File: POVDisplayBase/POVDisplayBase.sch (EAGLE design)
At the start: 35 parts, among them IC1 317EMP, IC2 STM32L052C8T, J1 FTSH-105, Q1 SSM3K329R, Q2 FQD10N20L, X1 MINI-USB-UX60-MB-5ST

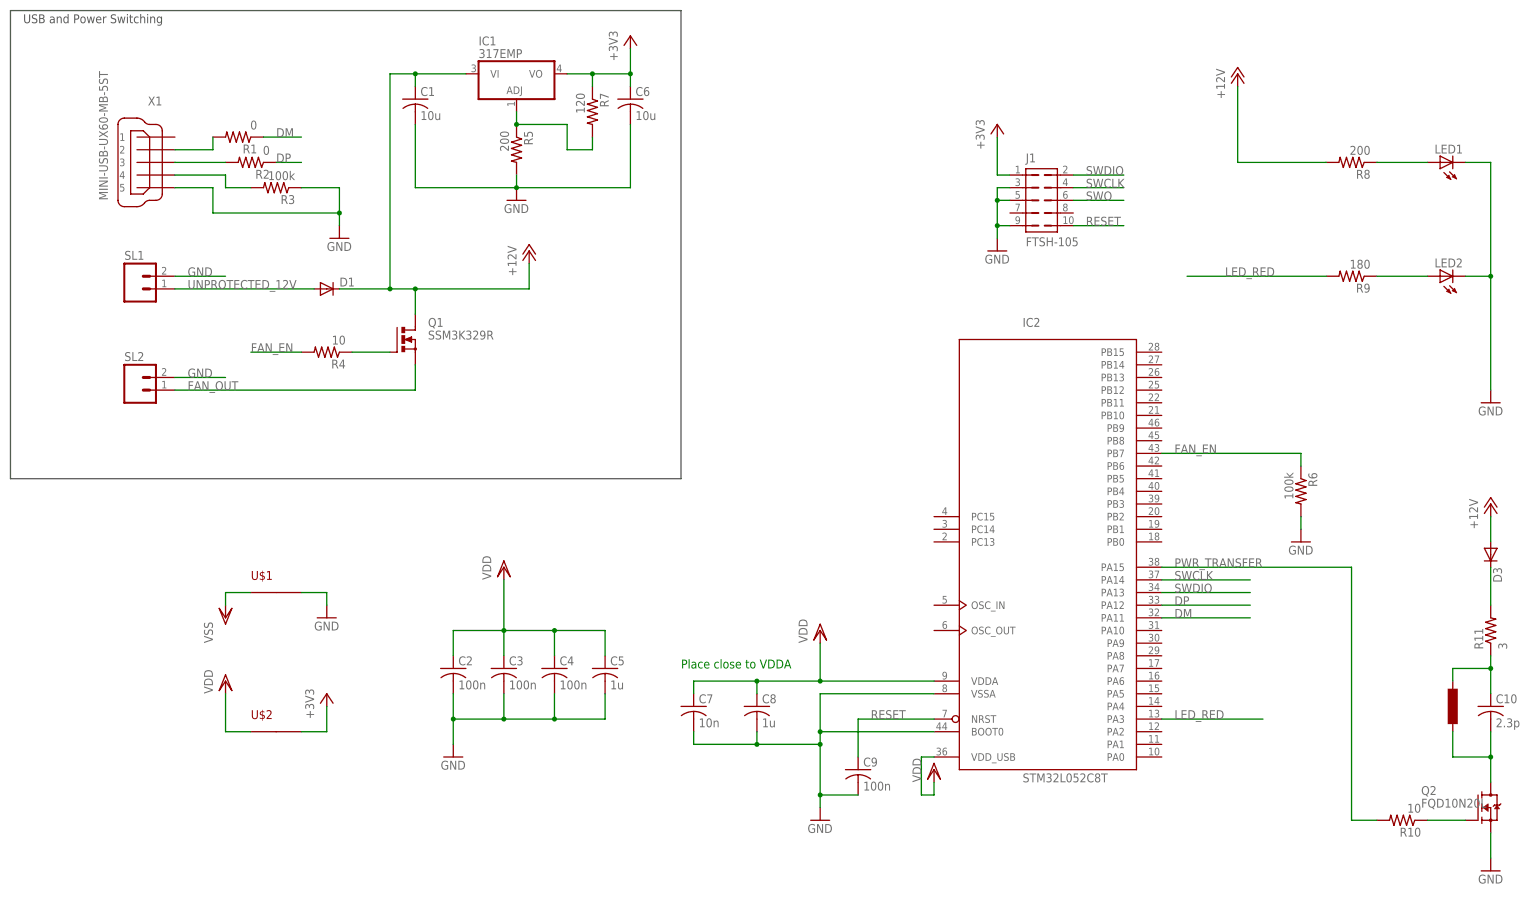
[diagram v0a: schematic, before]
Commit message: Removed the processor and simplified the POVDisplayBase
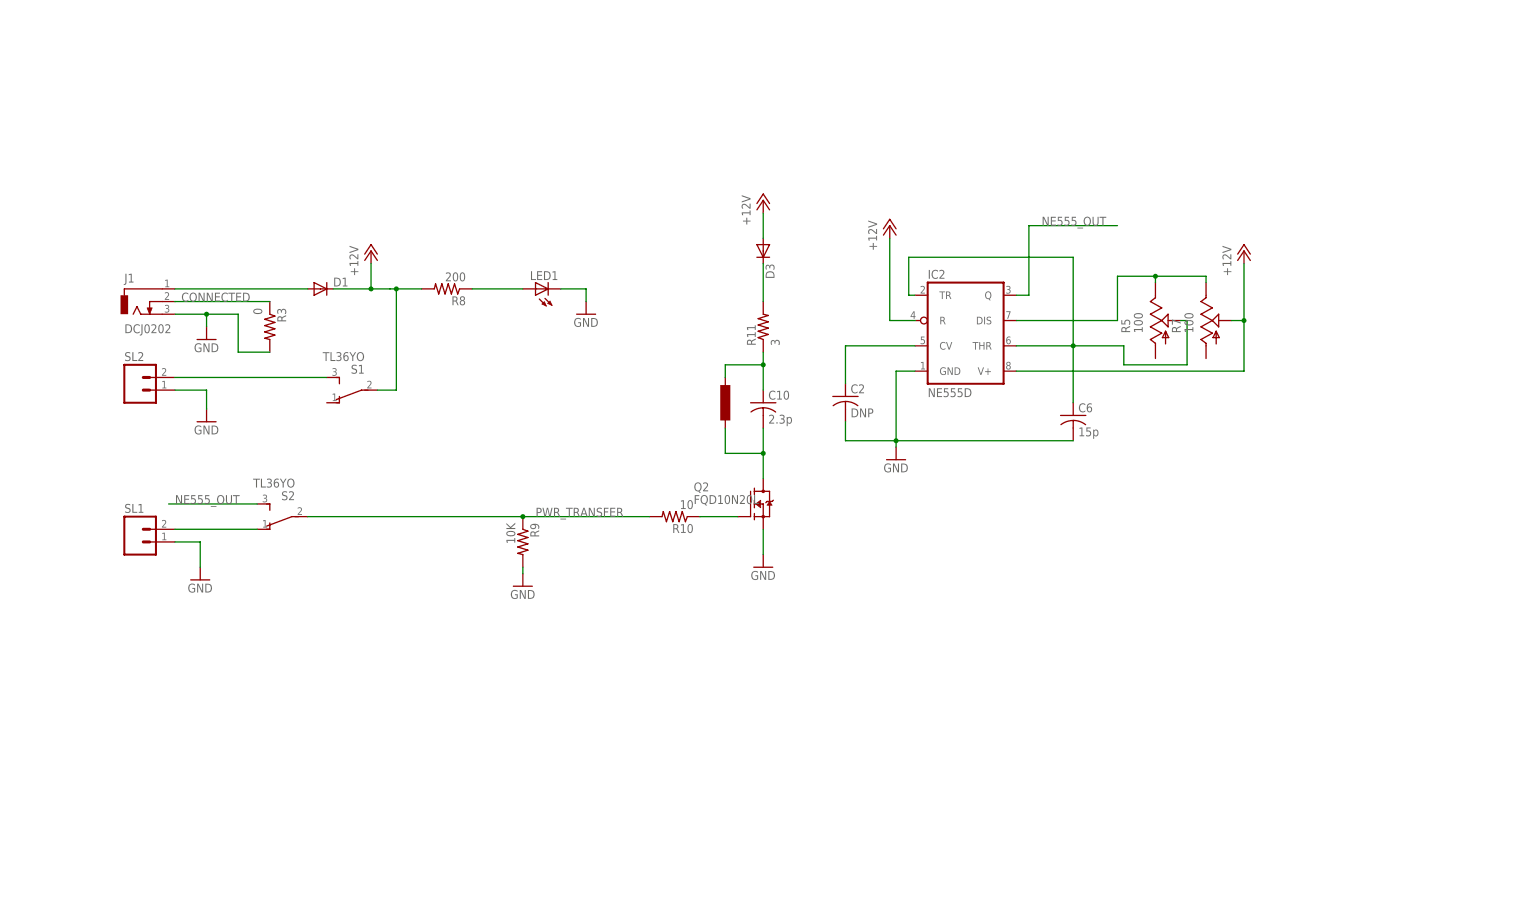
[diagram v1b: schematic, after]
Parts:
- removed C1: 10u, resistor:C-USC0603
- removed C3, C4, C9: 100n, resistor:C-USC0603
- removed C5, C8: 1u, resistor:C-USC0603
- removed C7: 10n, resistor:C-USC0603
- removed IC1: 317EMP, linear:317EMP
- removed LED2: (no value), led:LEDCHIP-LED0603
- removed Q1: SSM3K329R, NicksParts:SSM3K329R
- removed R1, R2: 0, resistor:R-US_R0603
- removed R4: 10, resistor:R-US_R0603
- removed R6: 100k, resistor:R-US_R0603
- removed U$1, U$2: SHORT, NicksParts:SHORT
- removed X1: MINI-USB-UX60-MB-5ST, con-hirose:MINI-USB-UX60-MB-5ST
- added S1, S2: TL36YO, switch:TL36YO
- C2: value 100n -> DNP
- C6: value 10u -> 15p
- IC2: value STM32L052C8T -> NE555D; device micro-stm_v2:STM32L052C8T -> linear:NE555D; DIGIKEY 497-14903-ND -> 296-6501-1-ND
- J1: value FTSH-105 -> DCJ0202; device NicksParts:FTSH-105 -> con-jack:DCJ0202; DIGIKEY SAM1161-50-ND -> CP-002B-ND; MATING_CONN (none) -> CP3-1001-ND
- R3: value 100k -> 0; DIGIKEY P100KGCT-ND -> P180GCT-ND
- R5: value 200 -> 100; device resistor:R-US_R0603 -> pot:TRIM_US-3223J; DIGIKEY P0.0GCT-ND -> A106082CT-ND
- R7: value 120 -> 100; device resistor:R-US_R0603 -> pot:TRIM_US-3223J; DIGIKEY P0.0GCT-ND -> A106082CT-ND
- R9: value 180 -> 10K
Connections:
- removed net +3V3: C6.1, IC1.VO, J1.1, R7.1, U$2.P$2
- removed net DM: IC2MCU.PA11, R1.1
- removed net DP: IC2MCU.PA12, R2.1
- removed net FAN_EN: IC2MCU.PB7, R4.2, R6.1
- removed net FAN_OUT: Q1.S, SL2.1
- removed net LED_RED: IC2MCU.PA3, R9.2
- removed net N$10: Q1.G, R4.1
- removed net N$6: R3.2, X1.4
- removed net N$7: IC1.ADJ, R5.1, R7.2
- removed net RESET: C9.1, IC2MCU.NRST, J1.10
- removed net SWCLK: IC2MCU.PA14, J1.4
- removed net SWDIO: IC2MCU.PA13, J1.2
- removed net SWO: J1.6
- removed net UNPROTECTED_12V: D1.A, SL1.1
- removed net VDD: C2.1, C3.1, C4.1, C5.1, C7.1, C8.1, IC2MCU.VDDA, IC2MCU.VDD_USB, U$2.P$1
- removed net VSS: U$1.P$1
- new net CONNECTED: J1.2, R3.1
- new net N$13: S2.O, SL1.2
- new net N$14: C2.1, IC2.CV
- new net N$3: S1.S, SL2.2
- new net NE555_OUT: IC2.Q, S2.S
- net +12V: now also IC2.R, IC2.V+, R7.S, S1.P; no longer C1.1, IC1.VI, Q1.D
- net GND: now also IC2.GND, R3.2, R9.2, SL1.1, SL2.1; no longer C1.2, C3.2, C4.2, C5.2, C7.2, C8.2, C9.2, IC2MCU.BOOT0, IC2MCU.VSSA, J1.5, J1.9, LED2.C, R3.1, R5.2, R6.2, SL1.2, SL2.2, U$1.P$2, X1.5
- net N$4: now also D1.A, J1.1; no longer R2.2, X1.3
- net N$5: now also C6.1, IC2.THR, IC2.TR, R5.S; no longer R1.2, X1.2
- net N$9: now also IC2.DIS, R5.E, R7.E; no longer LED2.A, R9.1
- net PWR_TRANSFER: now also R9.1, S2.P; no longer IC2MCU.PA15
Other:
- note removed: "Place close to VDDA"
- note removed: "USB and Power Switching"
- moved on the sheet: C10, C2, C6, D1, D3, LED1, Q2, R10, R11, R3, R8, R9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

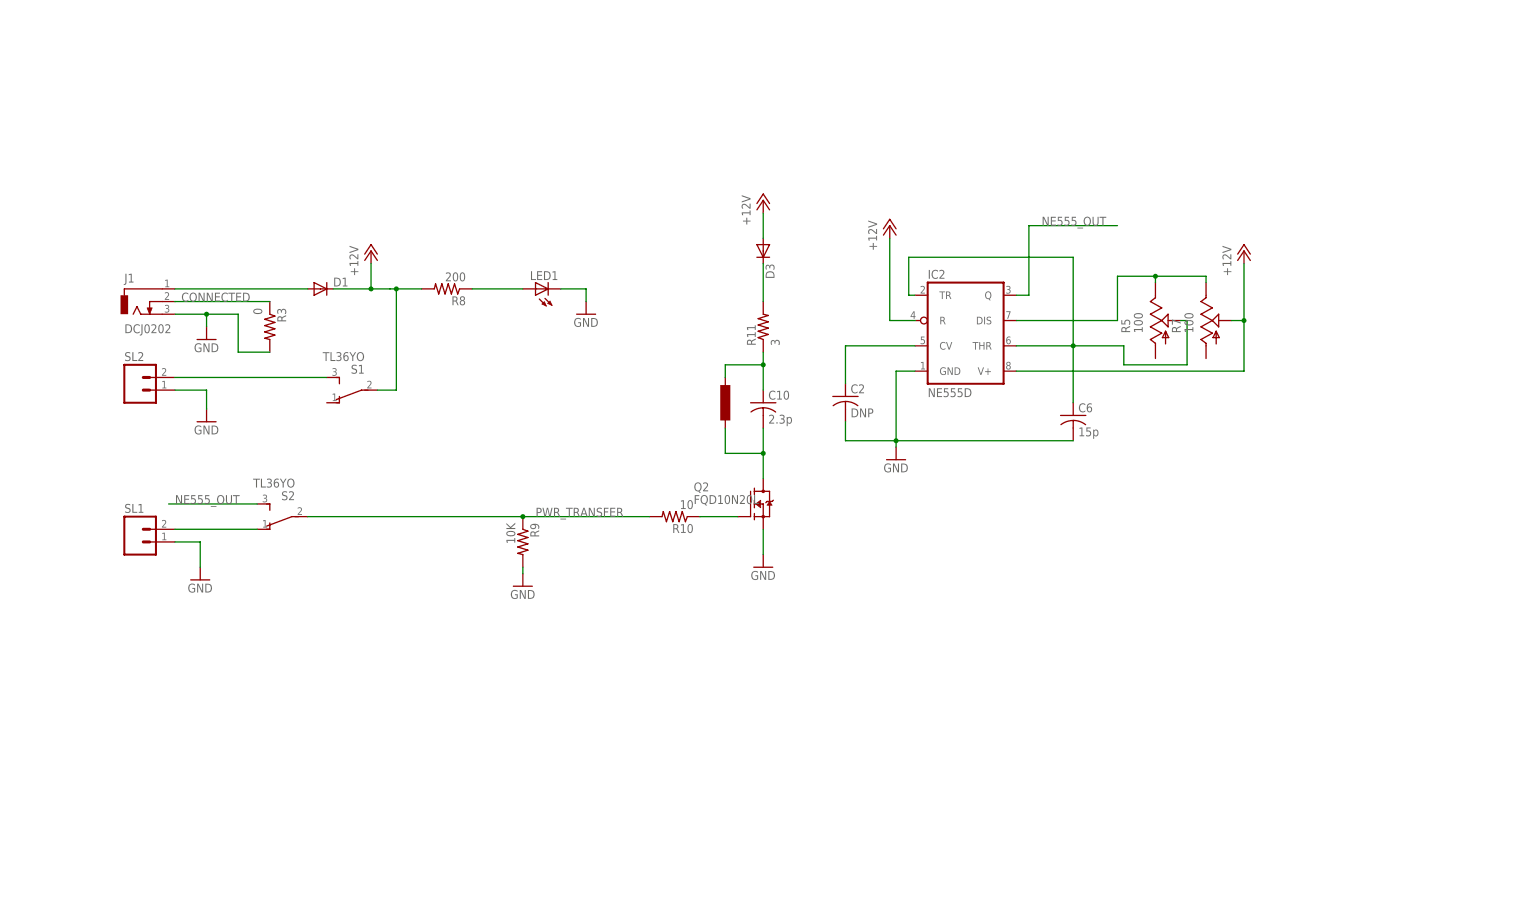
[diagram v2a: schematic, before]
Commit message: Updated the POVBase to use a PSoC, it is about the same price as a 555 and more flexible.
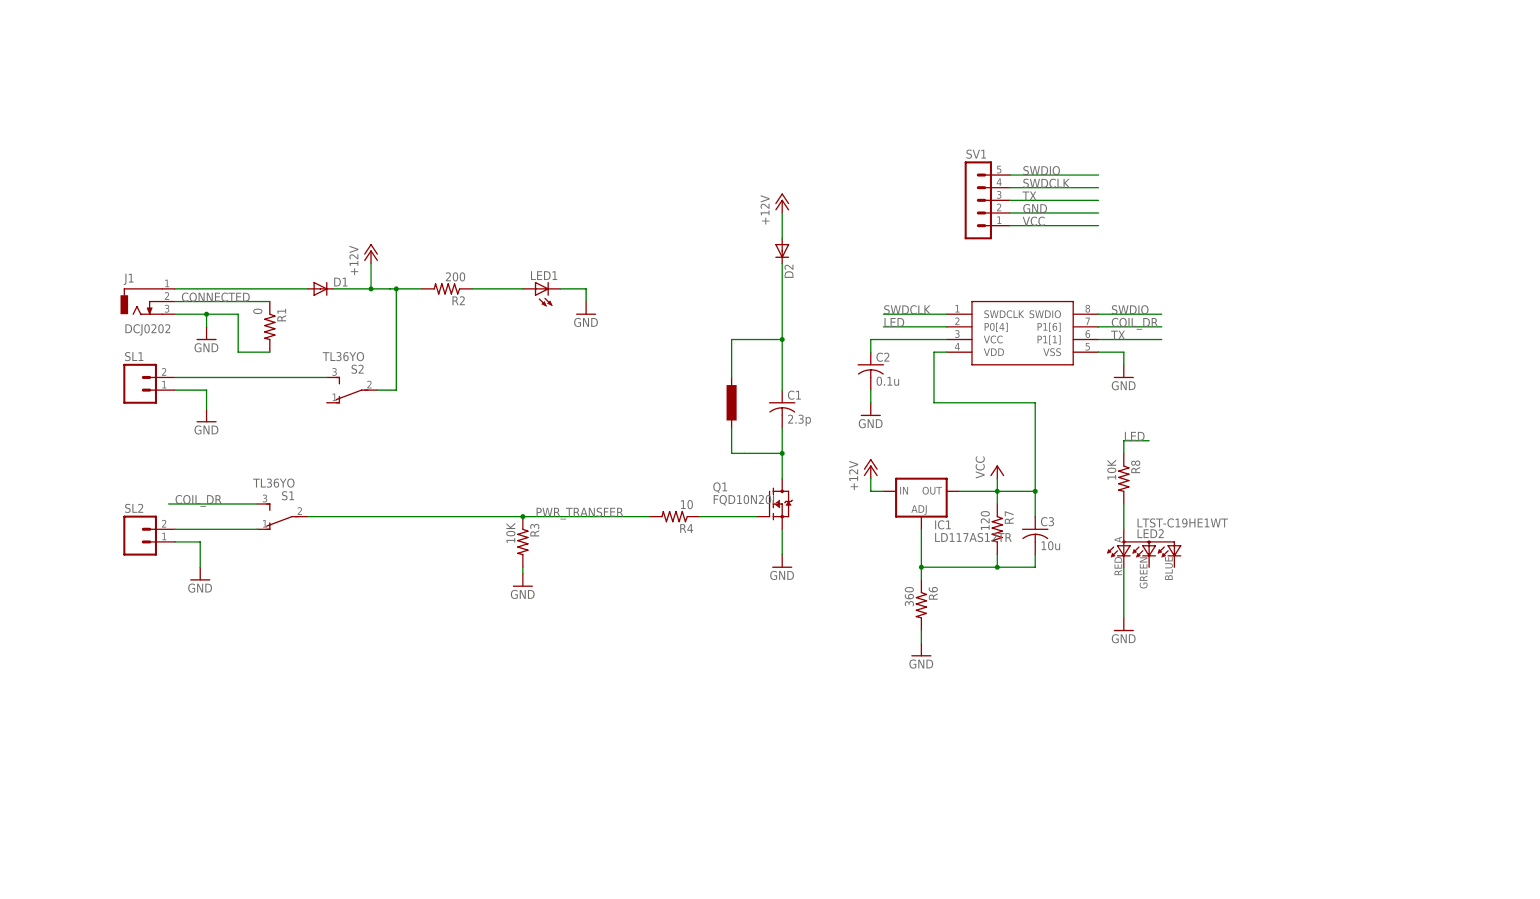
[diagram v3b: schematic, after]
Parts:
- removed C10: 2.3p, resistor:C-USC1210
- removed C6: 15p, resistor:C-USC0603
- removed D3: (no value), diode:DIODE-SMC
- removed IC2: NE555D, linear:NE555D
- removed Q2: FQD10N20L, NicksParts:FQD10N20L
- removed R11: 3, resistor:R-US_R1210
- removed R5: 100, pot:TRIM_US-3223J
- removed R9: 10K, resistor:R-US_R0603
- added C1: 2.3p, resistor:C-USC1210
- added C3: 10u, resistor:C-USC0603
- added D2: (no value), diode:DIODE-SMC
- added IC1: LD117AS12TR, v-reg:LD117AS12TR
- added LED2: LTST-C19HE1WT, NicksParts:LTST-C19HE1WT
- added Q1: FQD10N20L, NicksParts:FQD10N20L
- added R1: 0, resistor:R-US_R0603
- added R2: 200, resistor:R-US_R0603
- added R6: 360, resistor:R-US_R0603
- added SV1: (no value), con-lstb:MA05-1
- added U1: CY8C4013SXI-400, NicksParts:CY8C4013SXI-400
- C2: value DNP -> 0.1u
- R3: value 0 -> 10K
- R7: value 100 -> 120; device pot:TRIM_US-3223J -> resistor:R-US_R0603; DIGIKEY A106082CT-ND -> P180GCT-ND
- R8: value 200 -> 10K
- renumbered R10 to R4
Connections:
- removed net N$12: D3.C, R11.2
- removed net N$14: C2.1, IC2.CV
- removed net N$9: IC2.DIS, R5.E, R7.E
- removed net NE555_OUT: IC2.Q, S2.S
- new net COIL_DR: S1.S, U1.P1[6]
- new net LED: R8.1, U1.P0[4]
- new net N$6: LED2.A, R8.2
- new net N$7: C2.1, U1.VCC
- new net SWDCLK: SV1.4, U1.SWDCLK
- new net SWDIO: SV1.5, U1.SWDIO
- new net TX: SV1.3, U1.P1[1]
- new net VCC: C3.1, IC1.OUT, R7.1, SV1.1, U1.VDD
- net +12V: now also D2.A, IC1.IN, R2.2, S2.P; no longer D3.A, IC2.R, IC2.V+, R7.S, R8.2, S1.P
- net CONNECTED: now also R1.1; no longer R3.1
- net GND: now also LED2.CRED, Q1.S, R1.2, R6.2, SV1.2, U1.VSS; no longer C6.2, IC2.GND, Q2.S, R9.2
- net N$1: now also Q1.G; no longer Q2.G
- net N$13: now also S1.O, SL2.2; no longer S2.O, SL1.2
- net N$2: now also R2.1; no longer R8.1
- net N$3: now also S2.S, SL1.2; no longer S1.S, SL2.2
- net N$5: now also C3.2, IC1.ADJ, R6.1, R7.2; no longer C6.1, IC2.THR, IC2.TR, R5.S
- net NEG_COIL: now also C1.2, Q1.D; no longer C10.2, Q2.D
- net POS_COIL: now also C1.1, D2.C; no longer C10.1, R11.1
- net PWR_TRANSFER: now also R3.1, S1.P; no longer R9.1, S2.P
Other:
- moved on the sheet: C2, R3, R8, S1, S2, SL1, SL2
